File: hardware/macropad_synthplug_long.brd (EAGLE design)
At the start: 59.7 x 30.5 mm, 15 parts, among them IC1 H11L1MS, J1 SJ-3523-SMT, J2 SJ-3523-SMT

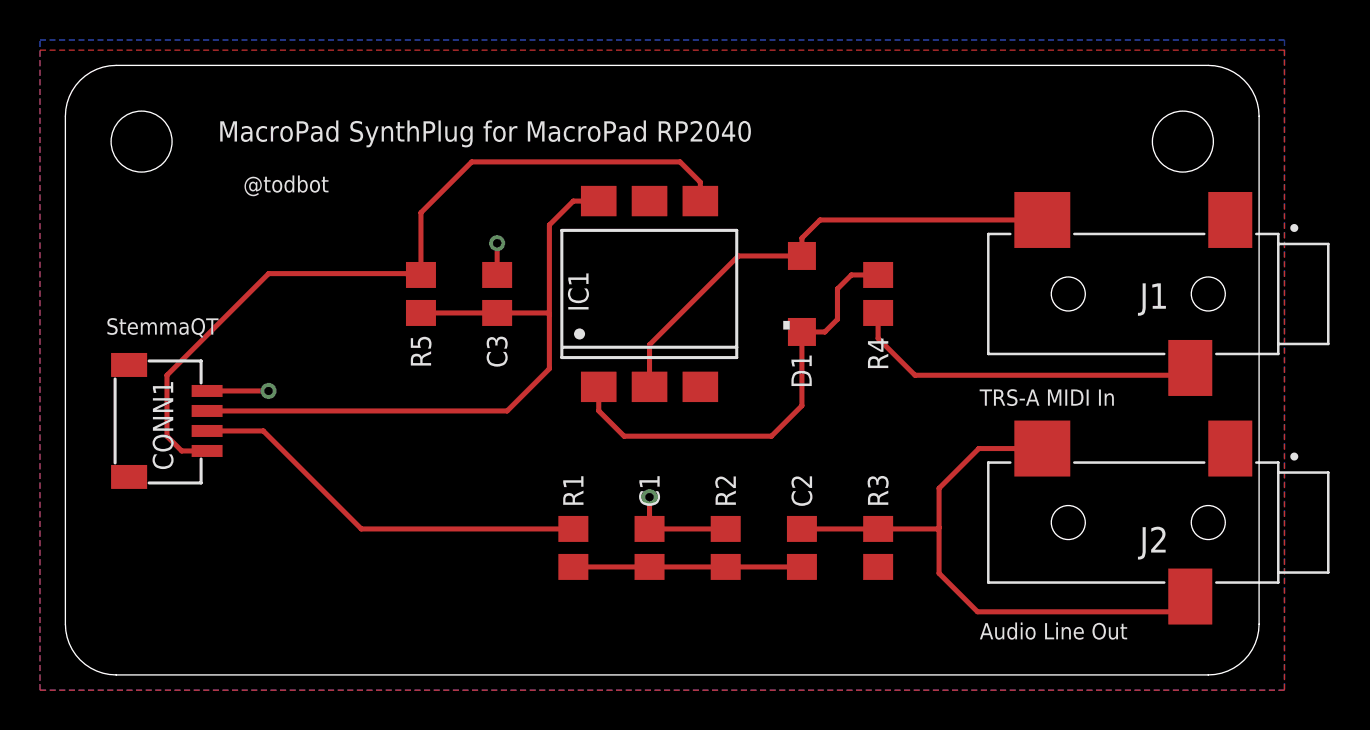
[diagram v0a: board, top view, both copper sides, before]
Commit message: submit long version to fab
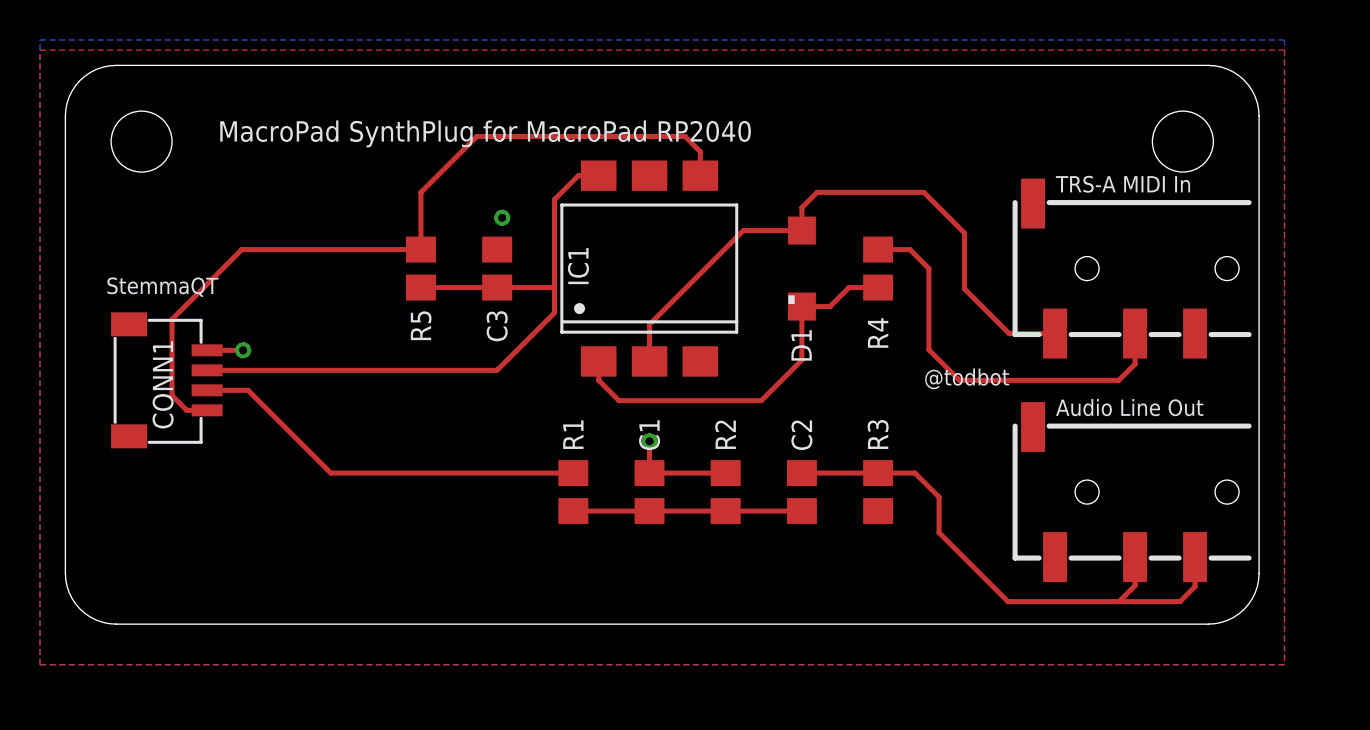
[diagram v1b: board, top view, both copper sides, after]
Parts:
- removed J1: SJ-3523-SMT, SJ-3523-SMT:CUI_SJ-3523-SMT
- added J3: AUDIO-JACK-TRRS, audio_jacks_todbot:PJ-320D_SPARKFUN
- J2: value SJ-3523-SMT -> AUDIO-JACK-TRRS; device SJ-3523-SMT:CUI_SJ-3523-SMT -> audio_jacks_todbot:PJ-320D_SPARKFUN
- moved U$2 6.40 mm to (44.5, 7.62)
- moved U$1 4.02 mm to (31.8, 10.2)
- moved J2 2.96 mm to (59.7, 9.14)
- moved C1 2.79 mm to (29.2, 9.14)
- moved C2 2.79 mm to (36.8, 9.14)
- moved R1 2.79 mm to (25.4, 9.14)
- moved R2 2.79 mm to (33.0, 9.14)
- moved R3 2.79 mm to (40.6, 9.14)
- moved CONN1 2.03 mm to (5.08, 14.7)
- moved C3 1.27 mm to (21.6, 20.3)
- moved D1 1.27 mm to (36.8, 20.3)
- moved IC1 1.27 mm to (29.2, 20.3)
- moved R4 1.27 mm to (40.6, 20.3), turned to 90 degrees
- moved R5 1.27 mm to (17.8, 20.3)
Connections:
- removed net N$15: J1.3, R4.2
- removed net N$47: C2.2, J2.2, J2.3, R3.1
- new net AUDIO_OUT: C2.2, J2.RING1, J2.RING2, R3.1
- new net N$2: J3.RING1, R4.2
- net GND: now also J2.EARTH, J3.EARTH; no longer J1.1, J2.1
- net N$14: now also J3.TIP; no longer J1.2
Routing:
- net N$47: track 30.8 -> 0.00 mm
- net AUDIO_OUT: track 0.00 -> 27.7 mm
- net N$2: track 0.00 -> 19.8 mm
- net N$15: track 17.8 -> 0.00 mm
- net N$14: track 24.9 -> 30.1 mm
- net GND: track 10.1 -> 7.20 mm
- net N$13: track 22.1 -> 19.2 mm
- net +3V3: track 34.6 -> 33.6 mm
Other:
- board size 59.7 x 30.5 mm -> 59.7 x 27.9 mm

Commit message: crap
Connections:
- net AUDIO_OUT: now also J2.TIP; no longer J2.RING2
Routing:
- net AUDIO_OUT: track 27.7 -> 24.4 mm
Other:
- board text added: "14 Jan 2023 - macropad_synthplug_long"
- board text removed: "4 Jan 2023 - macropad_synthplug_long"
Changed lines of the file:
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@@
 <dimension x1="-12.77611875" y1="30.58904375" x2="0" y2="2.54" x3="-23.3132375" y3="16.564521875" textsize="1.778" layer="47" dtype="vertical" unit="inch"/>
 <text x="12.7" y="11.684" size="1.016" layer="22" rot="MR0">StemmaQT / Qwiic</text>
-<text x="41.91" y="3.556" size="1.016" layer="22" rot="MR0">4 Jan 2023 - macropad_synthplug_long</text>
+<text x="41.91" y="3.556" size="1.016" layer="22" rot="MR0">14 Jan 2023 - macropad_synthplug_long</text>
 <text x="7.62" y="26.67" size="1.016" layer="21">MacroPad SynthPlug for MacroPad RP2040</text>
 </plain>
@@
 <wire x1="43.688" y1="7.112" x2="47.134" y2="3.666" width="0.254" layer="1"/>
 <contactref element="J2" pad="RING1"/>
-<contactref element="J2" pad="RING2"/>
 <wire x1="53.49" y1="4.468" x2="53.49" y2="5.894" width="0.254" layer="1"/>
-<wire x1="47.134" y1="3.666" x2="52.688" y2="3.666" width="0.254" layer="1"/>
+<wire x1="47.134" y1="3.666" x2="49.53" y2="3.666" width="0.254" layer="1"/>
+<wire x1="49.53" y1="3.666" x2="52.688" y2="3.666" width="0.254" layer="1"/>
 <wire x1="53.49" y1="4.468" x2="52.688" y2="3.666" width="0.254" layer="1"/>
-<wire x1="52.688" y1="3.666" x2="55.736" y2="3.666" width="0.254" layer="1"/>
-<wire x1="56.49" y1="4.42" x2="56.49" y2="5.894" width="0.254" layer="1"/>
-<wire x1="55.736" y1="3.666" x2="56.49" y2="4.42" width="0.254" layer="1"/>
 <wire x1="40.64" y1="10.094" x2="42.484" y2="10.094" width="0.254" layer="1"/>
 <wire x1="43.688" y1="8.89" x2="43.688" y2="7.112" width="0.254" layer="1"/>
 <wire x1="42.484" y1="10.094" x2="43.688" y2="8.89" width="0.254" layer="1"/>
+<contactref element="J2" pad="TIP"/>
+<wire x1="49.49" y1="5.894" x2="49.53" y2="5.854" width="0.254" layer="1"/>
+<wire x1="49.53" y1="5.854" x2="49.53" y2="3.666" width="0.254" layer="1"/>
 </signal>
 <signal name="N$48">

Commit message: get the trrs pinout right for realsies yeesh
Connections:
- net GND: now also J2.RING2
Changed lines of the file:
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@@
 <contactref element="J2" pad="EARTH"/>
 <contactref element="J3" pad="EARTH"/>
+<contactref element="J2" pad="RING2"/>
 </signal>
 <signal name="AUDIO_OUT">

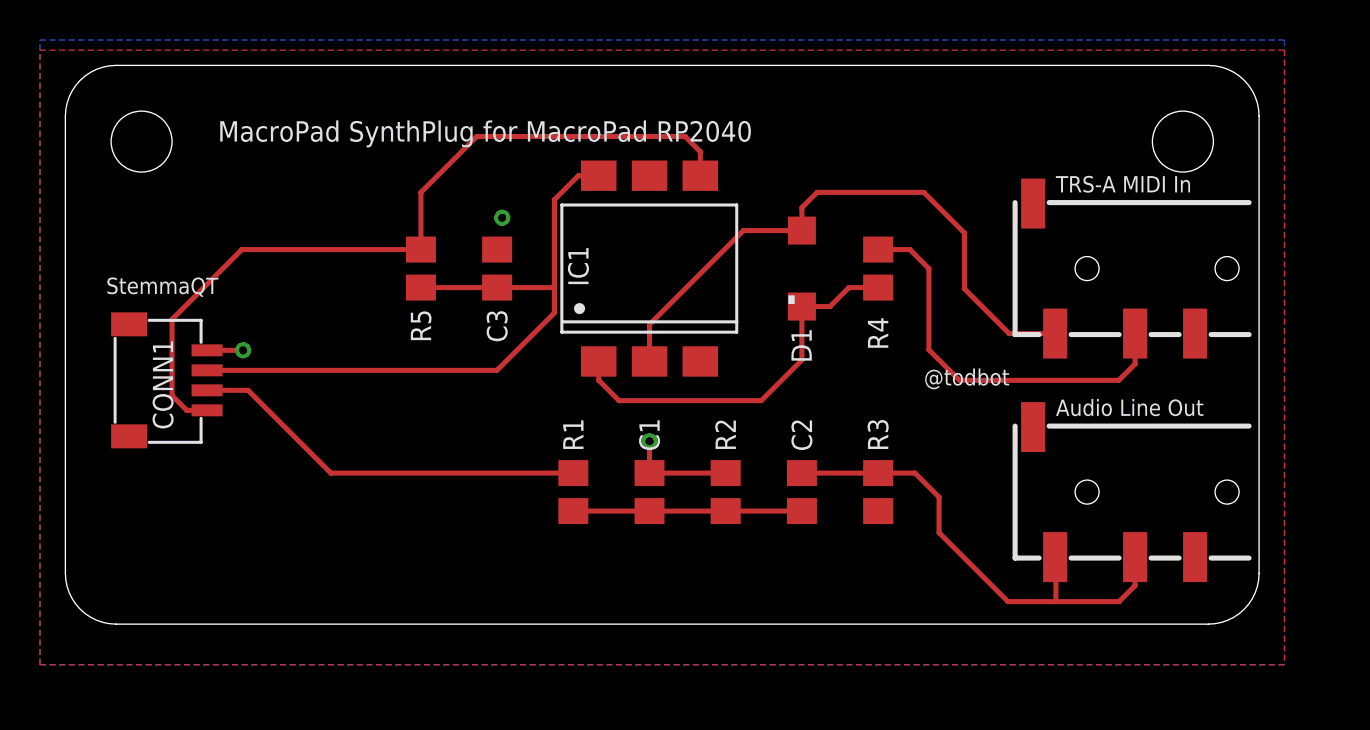
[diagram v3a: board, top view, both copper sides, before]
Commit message: cleanup silkscreen, send to fab
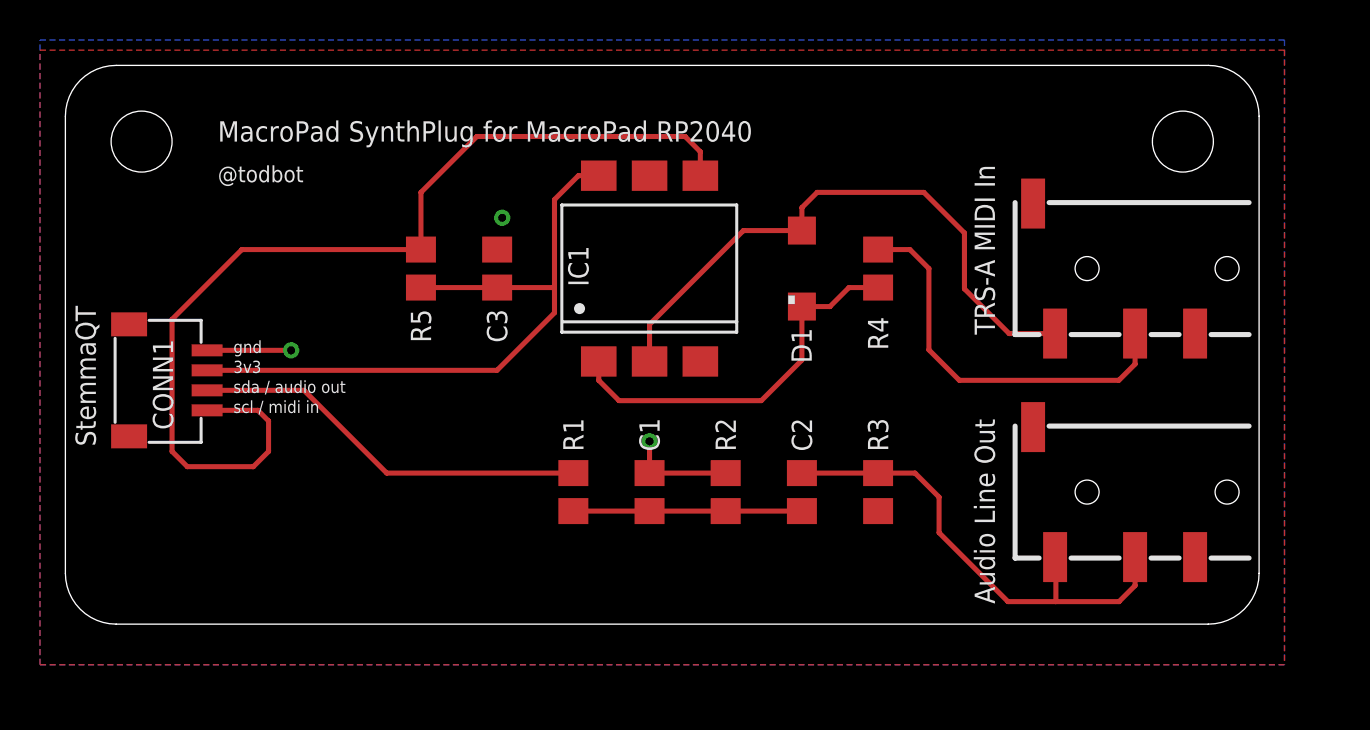
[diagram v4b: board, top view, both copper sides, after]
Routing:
- net MIDI_IN: track 39.3 -> 50.3 mm
- net GND: track 7.20 -> 9.60 mm
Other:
- board text added: "15 Jan 2023 - macropad_synthplug_long"
- board text added: "3v3"
- board text added: "gnd"
- board text added: "scl / midi in"
- board text added: "sda / audio out"
- board text removed: "14 Jan 2023 - macropad_synthplug_long"
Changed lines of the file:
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@@
 <setting verticaltext="up"/>
 </settings>
-<grid distance="0.05" unitdist="inch" unit="inch" style="lines" multiple="1" display="no" altdistance="0.01" altunitdist="inch" altunit="inch"/>
+<grid distance="0.1" unitdist="mm" unit="mm" style="lines" multiple="1" display="no" altdistance="1" altunitdist="mm" altunit="mm"/>
 <layers>
-<layer number="1" name="Top" color="4" fill="1" visible="yes" active="yes"/>
+<layer number="1" name="Top" color="4" fill="1" visible="no" active="yes"/>
 <layer number="2" name="Route2" color="16" fill="1" visible="no" active="no"/>
 <layer number="3" name="Route3" color="17" fill="1" visible="no" active="no"/>
@@
 <layer number="19" name="Unrouted" color="6" fill="1" visible="yes" active="yes"/>
 <layer number="20" name="Dimension" color="15" fill="1" visible="yes" active="yes"/>
-<layer number="21" name="tPlace" color="7" fill="1" visible="yes" active="yes"/>
+<layer number="21" name="tPlace" color="7" fill="1" visible="no" active="yes"/>
 <layer number="22" name="bPlace" color="7" fill="1" visible="yes" active="yes"/>
-<layer number="23" name="tOrigins" color="15" fill="1" visible="yes" active="yes"/>
+<layer number="23" name="tOrigins" color="15" fill="1" visible="no" active="yes"/>
 <layer number="24" name="bOrigins" color="15" fill="1" visible="yes" active="yes"/>
-<layer number="25" name="tNames" color="7" fill="1" visible="yes" active="yes"/>
+<layer number="25" name="tNames" color="7" fill="1" visible="no" active="yes"/>
 <layer number="26" name="bNames" color="7" fill="1" visible="yes" active="yes"/>
 <layer number="27" name="tValues" color="7" fill="1" visible="no" active="yes"/>
@@
 <layer number="37" name="tTest" color="7" fill="1" visible="no" active="yes"/>
 <layer number="38" name="bTest" color="7" fill="1" visible="no" active="yes"/>
-<layer number="39" name="tKeepout" color="4" fill="11" visible="yes" active="yes"/>
+<layer number="39" name="tKeepout" color="4" fill="11" visible="no" active="yes"/>
 <layer number="40" name="bKeepout" color="1" fill="11" visible="yes" active="yes"/>
-<layer number="41" name="tRestrict" color="4" fill="10" visible="yes" active="yes"/>
+<layer number="41" name="tRestrict" color="4" fill="10" visible="no" active="yes"/>
 <layer number="42" name="bRestrict" color="1" fill="10" visible="yes" active="yes"/>
 <layer number="43" name="vRestrict" color="2" fill="10" visible="no" active="yes"/>
 <layer number="44" name="Drills" color="7" fill="1" visible="no" active="yes"/>
-<layer number="45" name="Holes" color="7" fill="1" visible="yes" active="yes"/>
+<layer number="45" name="Holes" color="7" fill="1" visible="no" active="yes"/>
 <layer number="46" name="Milling" color="3" fill="1" visible="no" active="yes"/>
-<layer number="47" name="Measures" color="7" fill="1" visible="yes" active="yes"/>
-<layer number="48" name="Document" color="7" fill="1" visible="yes" active="yes"/>
-<layer number="49" name="Reference" color="7" fill="1" visible="yes" active="yes"/>
+<layer number="47" name="Measures" color="7" fill="1" visible="no" active="yes"/>
+<layer number="48" name="Document" color="7" fill="1" visible="no" active="yes"/>
+<layer number="49" name="Reference" color="7" fill="1" visible="no" active="yes"/>
 <layer number="50" name="dxf" color="7" fill="1" visible="no" active="no"/>
-<layer number="51" name="tDocu" color="7" fill="1" visible="yes" active="yes"/>
+<layer number="51" name="tDocu" color="7" fill="1" visible="no" active="yes"/>
 <layer number="52" name="bDocu" color="7" fill="1" visible="yes" active="yes"/>
 <layer number="53" name="tGND_GNDA" color="7" fill="9" visible="no" active="no"/>
@@
 <layer number="114" name="tPlaceRed" color="7" fill="1" visible="no" active="yes"/>
 <layer number="115" name="FRNTMAAT2" color="7" fill="1" visible="no" active="yes"/>
-<layer number="116" name="Patch_BOT" color="9" fill="4" visible="yes" active="yes"/>
+<layer number="116" name="Patch_BOT" color="9" fill="4" visible="no" active="yes"/>
 <layer number="117" name="BACKMAAT1" color="7" fill="1" visible="no" active="yes"/>
 <layer number="118" name="Rect_Pads" color="7" fill="1" visible="no" active="no"/>
@@
 <layer number="206" name="206bmp" color="7" fill="10" visible="no" active="yes"/>
 <layer number="207" name="207bmp" color="8" fill="10" visible="no" active="yes"/>
-<layer number="208" name="208bmp" color="9" fill="10" visible="yes" active="yes"/>
-<layer number="209" name="209bmp" color="7" fill="1" visible="yes" active="yes"/>
+<layer number="208" name="208bmp" color="9" fill="10" visible="no" active="yes"/>
+<layer number="209" name="209bmp" color="7" fill="1" visible="no" active="yes"/>
 <layer number="210" name="210bmp" color="7" fill="1" visible="no" active="yes"/>
 <layer number="211" name="211bmp" color="7" fill="1" visible="no" active="yes"/>
@@
 <plain>
 <wire x1="-2.54" y1="14.732" x2="66.04" y2="14.732" width="0.002540625" layer="49" style="shortdash"/>
-<text x="2.032" y="19.05" size="0.8128" layer="21">StemmaQT</text>
-<text x="49.53" y="12.954" size="0.8128" layer="21">Audio Line Out</text>
-<text x="49.53" y="24.13" size="0.8128" layer="21">TRS-A MIDI In</text>
+<text x="1.524" y="11.43" size="1.016" layer="21" ratio="12" rot="R90">StemmaQT</text>
+<text x="46.482" y="3.556" size="1.016" layer="21" ratio="12" rot="R90">Audio Line Out</text>
+<text x="46.482" y="17.018" size="1.016" layer="21" ratio="12" rot="R90">TRS-A MIDI In</text>
 <text x="35.814" y="18.542" size="2.54" layer="21" ratio="12">.</text>
-<text x="42.926" y="14.478" size="0.8128" layer="21">@todbot</text>
+<text x="7.62" y="24.638" size="0.8128" layer="21">@todbot</text>
 <text x="41.91" y="27.94" size="1.016" layer="22" rot="MR0">MacroPad RP2040 SynthPlug</text>
 <text x="41.91" y="22.86" size="1.016" layer="22" rot="MR0">@todbot</text>
@@
 <dimension x1="-12.77611875" y1="30.58904375" x2="0" y2="2.54" x3="-23.3132375" y3="16.564521875" textsize="1.778" layer="47" dtype="vertical" unit="inch"/>
 <text x="12.7" y="11.684" size="1.016" layer="22" rot="MR0">StemmaQT / Qwiic</text>
-<text x="41.91" y="3.556" size="1.016" layer="22" rot="MR0">14 Jan 2023 - macropad_synthplug_long</text>
-<text x="7.62" y="26.67" size="1.016" layer="21">MacroPad SynthPlug for MacroPad RP2040</text>
+<text x="41.91" y="3.556" size="1.016" layer="22" rot="MR0">15 Jan 2023 - macropad_synthplug_long</text>
+<text x="7.62" y="26.67" size="1.016" layer="21" ratio="12">MacroPad SynthPlug for MacroPad RP2040</text>
+<text x="8.4" y="16.1" size="0.6096" layer="21">gnd</text>
+<text x="8.4" y="15.1" size="0.6096" layer="21">3v3</text>
+<text x="8.4" y="14.1" size="0.6096" layer="21">sda / audio out</text>
+<text x="8.4" y="13.1" size="0.6096" layer="21">scl / midi in</text>
 </plain>
 <attributes>
@@
 <contactref element="C3" pad="2"/>
 <wire x1="29.21" y1="11.684" x2="29.21" y2="10.094" width="0.254" layer="1"/>
-<wire x1="8.89" y1="16.232" x2="7.086" y2="16.232" width="0.254" layer="1"/>
-<via x="8.89" y="16.232" extent="1-16" drill="0.4064"/>
+<wire x1="11.29" y1="16.232" x2="7.086" y2="16.232" width="0.254" layer="1"/>
+<via x="11.29" y="16.232" extent="1-16" drill="0.4064"/>
 <via x="21.844" y="22.86" extent="1-16" drill="0.4064"/>
 <contactref element="J2" pad="EARTH"/>
@@
 <contactref element="R1" pad="2"/>
 <contactref element="CONN1" pad="3"/>
-<wire x1="7.086" y1="14.232" x2="9.136" y2="14.232" width="0.254" layer="1"/>
-<wire x1="13.274" y1="10.094" x2="25.4" y2="10.094" width="0.254" layer="1"/>
-<wire x1="9.136" y1="14.232" x2="13.274" y2="10.094" width="0.254" layer="1"/>
+<wire x1="7.086" y1="14.232" x2="11.93" y2="14.232" width="0.254" layer="1"/>
+<wire x1="16.068" y1="10.094" x2="25.4" y2="10.094" width="0.254" layer="1"/>
+<wire x1="11.93" y1="14.232" x2="16.068" y2="10.094" width="0.254" layer="1"/>
 </signal>
 <signal name="MIDI_IN">
@@
 <contactref element="R5" pad="2"/>
 <contactref element="IC1" pad="4"/>
-<wire x1="7.086" y1="13.232" x2="6.07" y2="13.232" width="0.254" layer="1"/>
-<wire x1="6.07" y1="13.232" x2="5.334" y2="13.968" width="0.254" layer="1"/>
-<wire x1="5.334" y1="17.78" x2="5.334" y2="13.968" width="0.254" layer="1"/>
 <wire x1="30.988" y1="26.924" x2="31.75" y2="26.162" width="0.254" layer="1"/>
 <wire x1="31.75" y1="26.162" x2="31.75" y2="24.965" width="0.254" layer="1"/>
@@
 <wire x1="20.574" y1="26.924" x2="17.78" y2="24.13" width="0.254" layer="1"/>
 <wire x1="17.78" y1="21.27" x2="8.824" y2="21.27" width="0.254" layer="1"/>
-<wire x1="8.824" y1="21.27" x2="5.334" y2="17.78" width="0.254" layer="1"/>
+<wire x1="5.334" y1="17.78" x2="8.824" y2="21.27" width="0.254" layer="1"/>
+<wire x1="7.086" y1="13.232" x2="9.628" y2="13.232" width="0.254" layer="1"/>
+<wire x1="9.628" y1="13.232" x2="10.16" y2="12.7" width="0.254" layer="1"/>
+<wire x1="10.16" y1="12.7" x2="10.16" y2="11.176" width="0.254" layer="1"/>
+<wire x1="10.16" y1="11.176" x2="9.398" y2="10.414" width="0.254" layer="1"/>
+<wire x1="9.398" y1="10.414" x2="6.096" y2="10.414" width="0.254" layer="1"/>
+<wire x1="6.096" y1="10.414" x2="5.334" y2="11.176" width="0.254" layer="1"/>
+<wire x1="5.334" y1="11.176" x2="5.334" y2="17.78" width="0.254" layer="1"/>
 </signal>
 <signal name="+3V3">
